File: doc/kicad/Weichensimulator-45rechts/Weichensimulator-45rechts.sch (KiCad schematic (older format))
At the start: 9 parts, among them J1 Conn_01x02_Male, J2 Power, J3 Conn_01x02_Male, K1 HFD2_005-S-L2-D

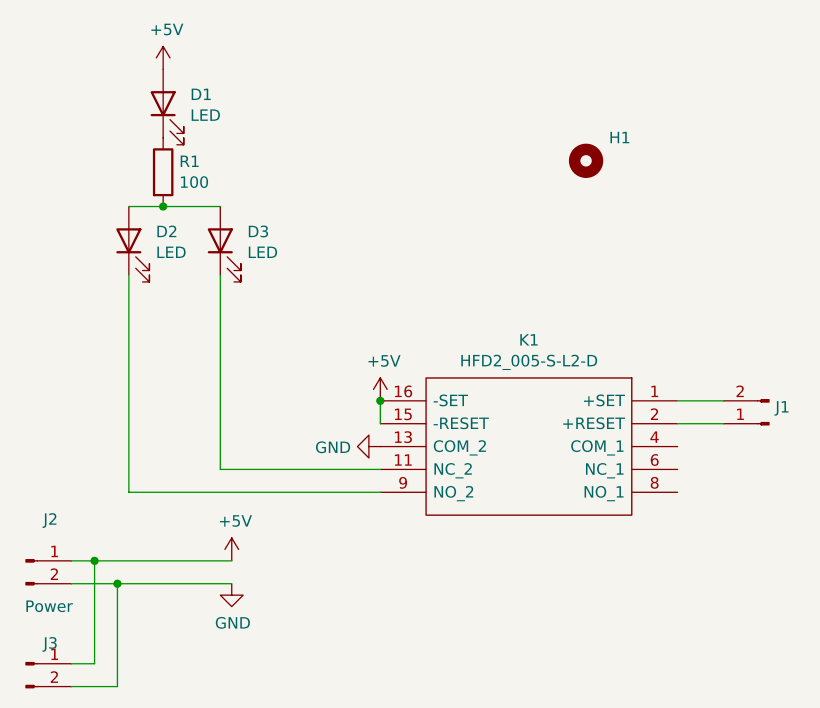
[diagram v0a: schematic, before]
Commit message: Bezeichnung nun auf der Besrückungsseite
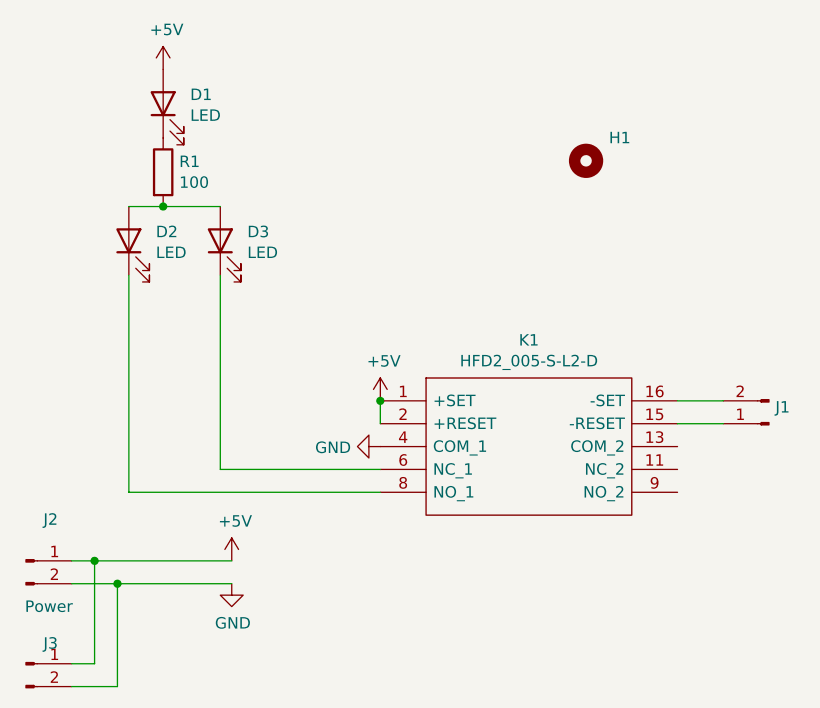
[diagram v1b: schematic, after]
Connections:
- net +5V: now also K1.1 (+SET), K1.2 (+RESET); no longer K1.15 (-RESET), K1.16 (-SET)
- net GND: now also K1.4 (COM_1); no longer K1.13 (COM_2)
- net at D2.1 (K): now also K1.8 (NO_1); no longer K1.9 (NO_2)
- net at D3.1 (K): now also K1.6 (NC_1); no longer K1.11 (NC_2)
- net at J1.2 (Pin_2): now also K1.16 (-SET); no longer K1.1 (+SET)
- net at J1.1 (Pin_1): now also K1.15 (-RESET); no longer K1.2 (+RESET)
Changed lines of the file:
@@
 L HFD2_005-S-L2-D:HFD2_005-S-L2-D K1
 U 1 1 6125B40D
-P 6750 3150
-F 0 "K1" H 7400 3415 50  0000 C CNN
-F 1 "HFD2_005-S-L2-D" H 7400 3324 50  0000 C CNN
-F 2 "HFD2005SL2D" H 7900 3250 50  0001 L CNN
-F 3 "http://www.hongfa.com/pro/pdf/HFD2_en.pdf" H 7900 3150 50  0001 L CNN
-F 4 "Hongfa Europe GMBH DPDT Non-Latching Relay PCB Mount, 5V dc Coil, 3 A, 3 A Subminiature DIP Relay" H 7900 3050 50  0001 L CNN "Description"
-F 5 "10.6" H 7900 2950 50  0001 L CNN "Height"
-F 6 "Hongfa" H 7900 2850 50  0001 L CNN "Manufacturer_Name"
-F 7 "HFD2/005-S-L2-D" H 7900 2750 50  0001 L CNN "Manufacturer_Part_Number"
-F 8 "" H 7900 2650 50  0001 L CNN "Mouser Part Number"
-F 9 "" H 7900 2550 50  0001 L CNN "Mouser Price/Stock"
-F 10 "HFD2/005-S-L2-D" H 7900 2450 50  0001 L CNN "Arrow Part Number"
-F 11 "https://www.arrow.com/en/products/hfd2005-s-l2-d/hongfa-europe-gmbh" H 7900 2350 50  0001 L CNN "Arrow Price/Stock"
-	1    6750 3150
-	-1   0    0    -1
+P 5450 3150
+F 0 "K1" H 6100 3415 50  0000 C CNN
+F 1 "HFD2_005-S-L2-D" H 6100 3324 50  0000 C CNN
+F 2 "HFD2005SL2D" H 6600 3250 50  0001 L CNN
+F 3 "http://www.hongfa.com/pro/pdf/HFD2_en.pdf" H 6600 3150 50  0001 L CNN
+F 4 "Hongfa Europe GMBH DPDT Non-Latching Relay PCB Mount, 5V dc Coil, 3 A, 3 A Subminiature DIP Relay" H 6600 3050 50  0001 L CNN "Description"
+F 5 "10.6" H 6600 2950 50  0001 L CNN "Height"
+F 6 "Hongfa" H 6600 2850 50  0001 L CNN "Manufacturer_Name"
+F 7 "HFD2/005-S-L2-D" H 6600 2750 50  0001 L CNN "Manufacturer_Part_Number"
+F 8 "" H 6600 2650 50  0001 L CNN "Mouser Part Number"
+F 9 "" H 6600 2550 50  0001 L CNN "Mouser Price/Stock"
+F 10 "HFD2/005-S-L2-D" H 6600 2450 50  0001 L CNN "Arrow Part Number"
+F 11 "https://www.arrow.com/en/products/hfd2005-s-l2-d/hongfa-europe-gmbh" H 6600 2350 50  0001 L CNN "Arrow Price/Stock"
+	1    5450 3150
+	1    0    0    -1
 $EndComp
 $Comp
@@
 Wire Wire Line
 	6750 3250 6950 3250
-Wire Wire Line
-	4100 3850 4200 3850
-Wire Wire Line
-	4100 3950 4300 3950
 $Comp
 L power:+5V #PWR0103
@@
 Wire Wire Line
 	5450 3250 5450 3150
-Connection ~ 4200 3850
 Wire Wire Line
 	4200 3850 4800 3850
-Connection ~ 4300 3950
 Wire Wire Line
 	4300 3950 4800 3950
-Connection ~ 5450 3150
 Wire Wire Line
 	4350 2300 4500 2300
@@
 	1    0    0    -1
 $EndComp
+Connection ~ 5450 3150
+Connection ~ 4300 3950
+Connection ~ 4200 3850
 $Comp
 L Connector:Conn_01x02_Male J2
@@
 	1    0    0    -1
 $EndComp
+Wire Wire Line
+	4100 3950 4300 3950
+Wire Wire Line
+	4100 3850 4200 3850
 $EndSCHEMATC
